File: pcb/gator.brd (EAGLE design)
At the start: 101.6 x 81.3 mm, 70 parts, among them J2 POWER_JACKPTH

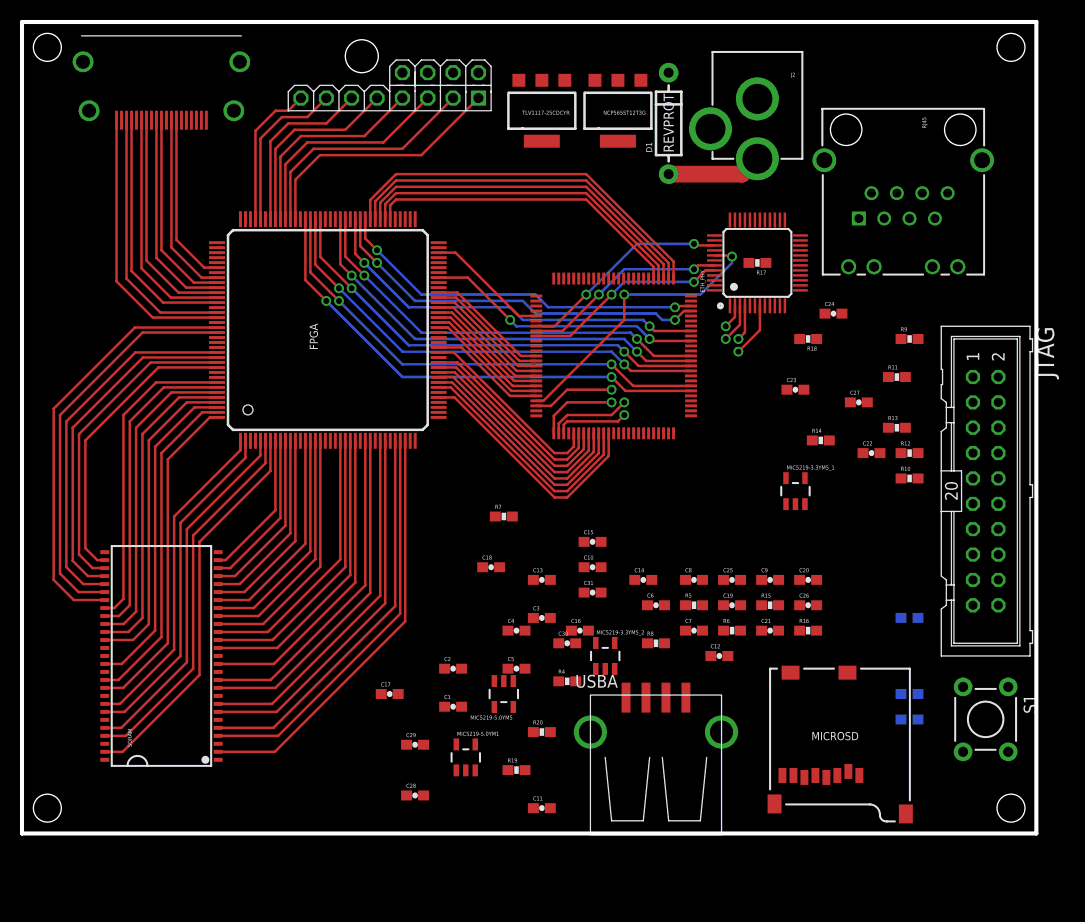
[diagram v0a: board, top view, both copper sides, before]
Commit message: Cleaned up power supplies and connected usb and micro sd
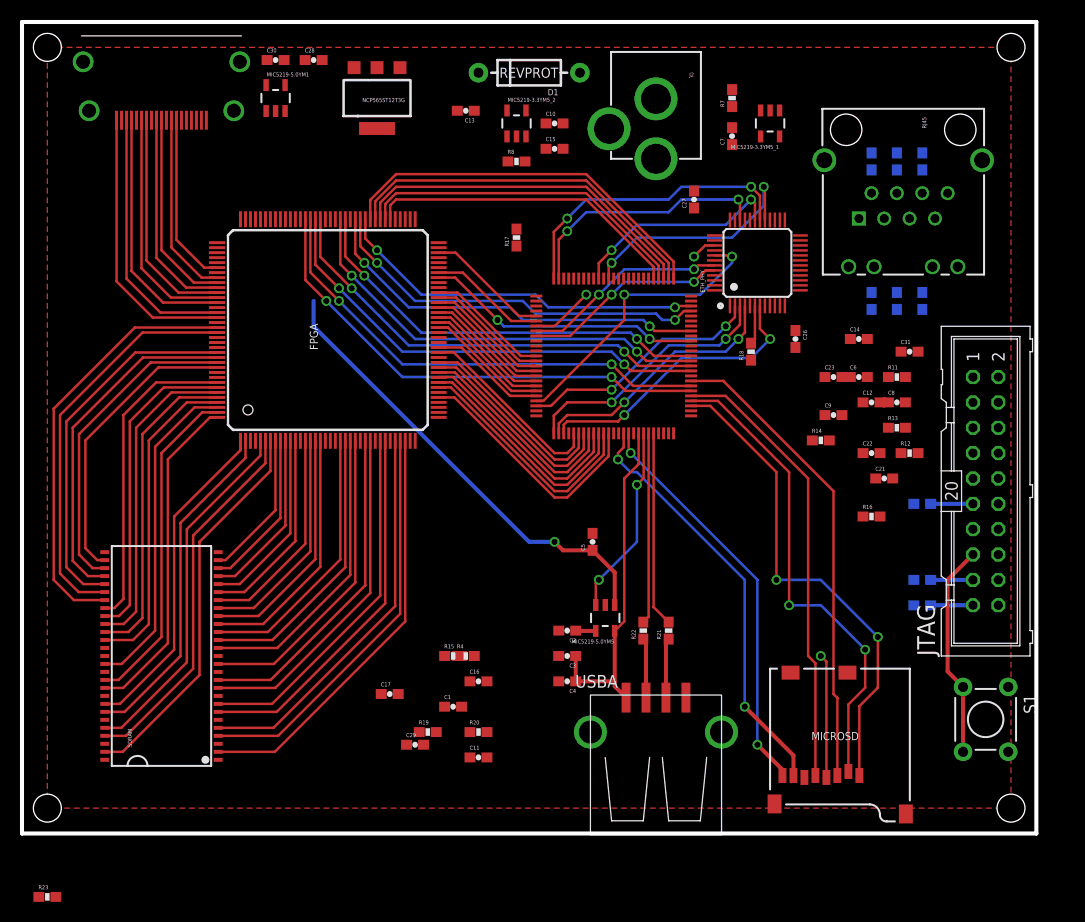
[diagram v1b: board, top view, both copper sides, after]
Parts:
- removed C18, C20: 100n, SparkFun-Passives:0603-CAP
- removed C19: 2.2u, SparkFun-Passives:0603-CAP
- removed TLV1117-25CDCYR: (no value), microbuilder:SOT223-R
- removed U$3: WING8, Papilio:WINGSIDE_8BIT
- added R21, R22: 22, SparkFun-Passives:0603-RES
- added R23: 10K, SparkFun-Passives:0603-RES
- moved C28 74.4 mm to (29.2, 77.5)
- moved MIC5219-5.0YM1 68.7 mm to (25.4, 73.7)
- moved C30 65.3 mm to (25.4, 77.5)
- moved MIC5219-3.3YM5_2 54.1 mm to (49.5, 71.1)
- moved R8 50.2 mm to (49.5, 67.3)
- moved R5 50.0 mm to (90.2, 67.3), flipped to the bottom, turned to 270 degrees
- moved R6 49.8 mm to (87.6, 67.3), flipped to the bottom, turned to 270 degrees
- moved C7 49.7 mm to (71.1, 69.8), turned to 90 degrees
- moved R7 47.7 mm to (71.1, 73.7), turned to 90 degrees
- moved C13 47.6 mm to (44.5, 72.4), turned to 180 degrees
- moved C10 44.6 mm to (53.3, 71.1)
- moved C25 44.2 mm to (85.1, 67.3), flipped to the bottom, turned to 90 degrees
- moved C31 39.9 mm to (88.9, 48.3)
- moved C15 39.6 mm to (53.3, 68.6)
- moved MIC5219-3.3YM5_1 36.9 mm to (74.9, 71.1), turned to 180 degrees
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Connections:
- removed net N$23: FPGA.P102, U$3.5
- removed net N$24: FPGA.P99, U$3.2
- removed net N$25: FPGA.P100, U$3.3
- removed net N$26: FPGA.P97, U$3.0
- removed net N$27: FPGA.P98, U$3.1
- removed net TCLK/SWCLK: JTAG.9
- removed net VCC/2: C19.1, C20.1, TLV1117-25CDCYR.2
- removed net VSS: U$1.10, U$1.27, U$1.74, U$1.99
- removed net VSSA: U$1.20
- new net SPI_MISO: FPGA.P66, U$1.31
- net +3V3: now also SDRAM.1, SDRAM.14, SDRAM.27, SDRAM.3, SDRAM.43, SDRAM.49, SDRAM.9
- net GND: now also SDRAM.12, SDRAM.28, SDRAM.41, SDRAM.46, SDRAM.52, SDRAM.54, SDRAM.6, U$1.10, U$1.20, U$1.27, U$1.74, U$1.99; no longer C18.2, C19.2, C20.2, TLV1117-25CDCYR.1
- net N$1: now also R21.2; no longer USBA.D+
- net N$19: now also R21.1, USBA.D+; no longer FPGA.P104, U$3.6
- net N$2: now also R22.2; no longer USBA.D-
- net N$20: now also R22.1, USBA.D-; no longer FPGA.P105, U$3.7
- net N$21: now also MIC5219-5.0YM1.3, R23.1; no longer FPGA.P101, U$3.4
- net TCK/SWCLK: now also JTAG.9
- net USB_EN: no longer MIC5219-5.0YM1.3
- net V+: now also R23.2; no longer C18.1, TLV1117-25CDCYR.3
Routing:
- net SD_D2: track 0.00 -> 49.3 mm, vias 0 -> 2
- net SD_D3: track 0.00 -> 48.5 mm, vias 0 -> 2
- net SD_CMD: track 0.00 -> 47.5 mm
- net V+: track 0.00 -> 46.2 mm, vias 0 -> 1
- net NRST: track 0.00 -> 46.0 mm, vias 0 -> 2
- net SD_CLK: track 0.00 -> 45.2 mm
- net SD_D0: track 0.00 -> 42.2 mm, vias 0 -> 2
- net SD_D1: track 0.00 -> 40.7 mm, vias 0 -> 2
- net USB_VBUS: track 0.00 -> 34.4 mm
- net MII_MDIO: track 0.00 -> 30.0 mm, vias 0 -> 2
- net N$26: track 25.7 -> 0.00 mm
- net 50MHZ_OSC: track 0.00 -> 25.7 mm, vias 0 -> 2
- net N$27: track 24.1 -> 0.00 mm
- net N$24: track 22.5 -> 0.00 mm
- net MII_MDC: track 0.00 -> 21.7 mm, vias 0 -> 2
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- added copper zone on layer 1, net GND

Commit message: more power supply cleanup
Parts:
- moved R23 83.1 mm to (29.2, 72.4)
- moved C11 62.2 mm to (44.5, 69.8), turned to 180 degrees
- moved R19 59.9 mm to (19.1, 66.0), turned to 90 degrees
- moved R20 59.1 mm to (17.8, 62.2)
- moved C16 55.0 mm to (27.9, 67.3)
- moved C6 51.8 mm to (41.9, 76.2), turned to 90 degrees
- moved R4 50.2 mm to (92.7, 3.81), turned to 180 degrees
- moved C21 34.3 mm to (64.8, 62.2), turned to 90 degrees
- moved R12 34.1 mm to (73.7, 68.6), turned to 180 degrees
- moved R16 33.9 mm to (77.5, 64.8)
- moved C9 33.1 mm to (78.7, 74.9), turned to 90 degrees
- moved R14 22.6 mm to (97.8, 53.3), turned to 270 degrees
- moved C17 16.1 mm to (41.9, 29.2)
- moved R13 13.3 mm to (91.4, 53.3), turned to 270 degrees
- moved R11 9.16 mm to (82.5, 53.3), turned to 270 degrees
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
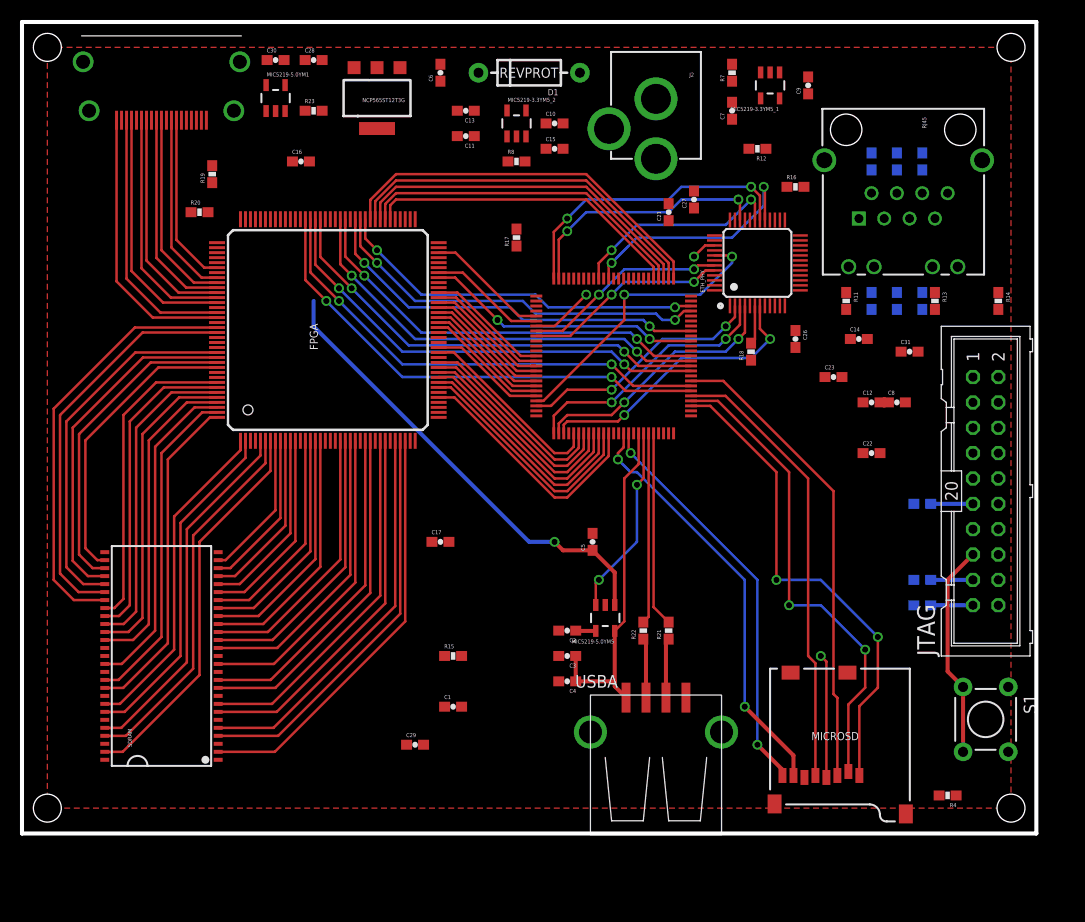
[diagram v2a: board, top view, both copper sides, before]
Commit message: Added HDMI termination, oscillators, improved routing
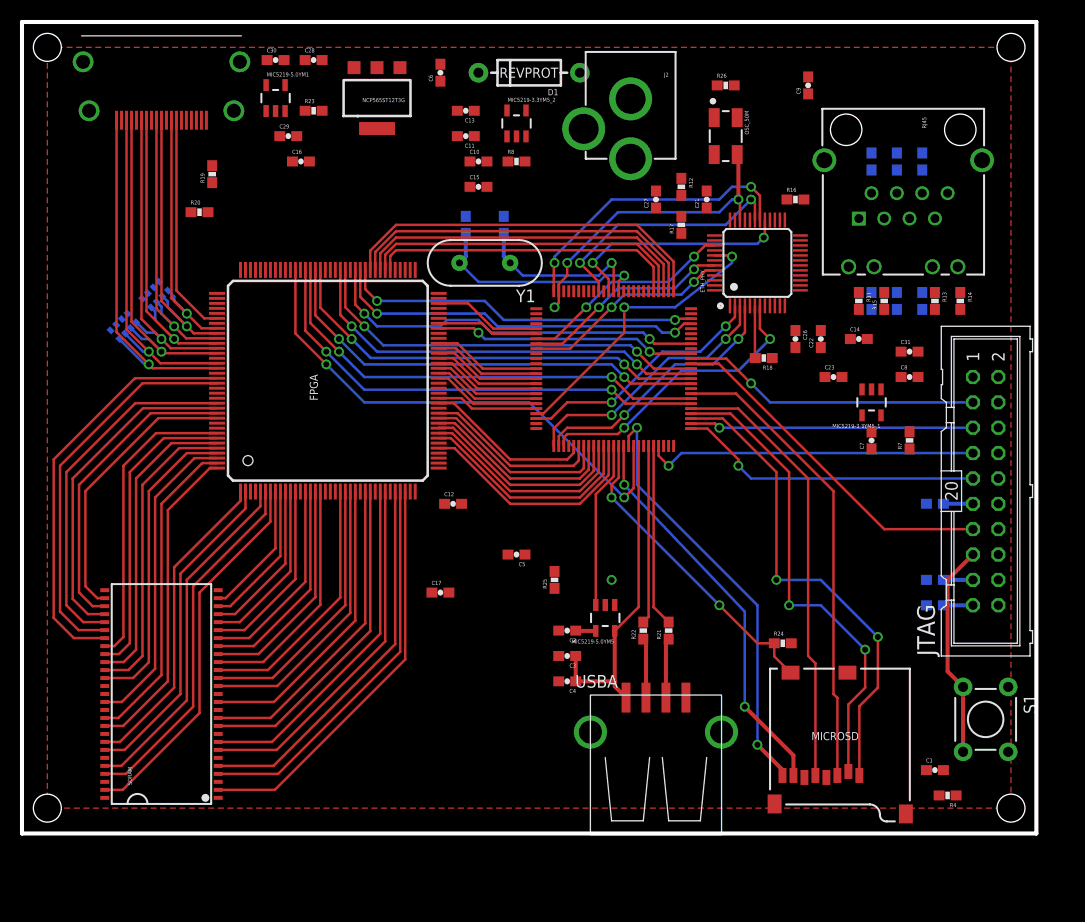
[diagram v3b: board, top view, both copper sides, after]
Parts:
- added C18, C19: 20p, SparkFun-Passives:0603-CAP
- added OSC_50M: OSCILLATOR5X3-PIN1-INDICATED, SparkFun-FreqCtrl:CRYSTAL-OSC-SMD-5X3
- added R24, R25: 10K, SparkFun-Passives:0603-RES
- added R26: 2K2, SparkFun-Passives:0603-RES
- added R27, R28: 51, SparkFun-Passives:0603-ARV
- added Y1: 12MHz, SparkFun-FreqCtrl:HC49US
- moved C29 62.3 mm to (26.7, 69.8)
- moved R15 55.9 mm to (86.4, 53.3), turned to 90 degrees
- moved C1 48.7 mm to (91.4, 6.35)
- moved C12 43.1 mm to (43.2, 33.0)
- moved R7 40.9 mm to (88.9, 39.4)
- moved C7 35.9 mm to (85.1, 39.4)
- moved MIC5219-3.3YM5_1 33.3 mm to (85.1, 43.2)
- moved R17 16.6 mm to (66.0, 61.0)
- moved C22 12.5 mm to (80.0, 49.5), turned to 90 degrees
- moved C10 8.52 mm to (45.7, 67.3)
- moved C15 8.52 mm to (45.7, 64.8)
- moved R12 8.52 mm to (66.0, 64.8), turned to 270 degrees
- moved C5 7.73 mm to (49.5, 27.9), turned to 180 degrees
- moved C17 5.08 mm to (41.9, 24.1)
- moved FPGA 5.08 mm to (30.6, 45.3)
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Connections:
- new net FPGA_CLK1: FPGA.P97, U$1.67
- new net FPGA_CLK2: FPGA.P98
- new net N$29: C18.1, U$1.12, Y1.2
- new net N$30: C19.1, U$1.13, Y1.1
- new net N$31: OSC_50M.1, R26.1
- new net SD_DETECT: MICROSD.CD1, R24.1, U$1.64
- net +3V3: now also OSC_50M.4, R24.2, R26.2; no longer FPGA.P103, FPGA.P122, FPGA.P125, FPGA.P129, FPGA.P135, FPGA.P18, FPGA.P20, FPGA.P31, FPGA.P36, FPGA.P4, FPGA.P42, FPGA.P53, FPGA.P63, FPGA.P76, FPGA.P86, FPGA.P90
- net 50MHZ_OSC: now also OSC_50M.3
- net GND: now also C18.2, C19.2, OSC_50M.2
- net TMDS_CLKN: now also R27.1
- net TMDS_CLKP: now also R27.2
- net TMDS_D0N: now also R27.3
- net TMDS_D0P: now also R27.4
- net TMDS_D1N: now also R28.1
- net TMDS_D1P: now also R28.2
- net TMDS_D2N: now also R28.3
- net TMDS_D2P: now also R28.4
- net USB_EN: now also R25.1, U$1.63; no longer U$1.69
- net V+: now also R25.2
- net VCCIO: now also FPGA.P103, FPGA.P122, FPGA.P125, FPGA.P129, FPGA.P135, FPGA.P18, FPGA.P20, FPGA.P31, FPGA.P36, FPGA.P4, FPGA.P42, FPGA.P53, FPGA.P63, FPGA.P76, FPGA.P86, FPGA.P90, R27.5, R27.6, R27.7, R27.8, R28.5, R28.6, R28.7, R28.8
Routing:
- net FPGA_CLK1: track 0.00 -> 51.7 mm, vias 0 -> 2
- net V+: track 46.2 -> 0.00 mm
- net TDO/SWO: track 0.00 -> 35.1 mm
- net TMS/SWDIO: track 0.00 -> 33.4 mm, vias 0 -> 1
- net SD_DETECT: track 0.00 -> 31.4 mm, vias 0 -> 2
- net TCK/SWCLK: track 0.00 -> 30.7 mm, vias 0 -> 1
- net /TRST: track 0.00 -> 30.1 mm, vias 0 -> 1
- net TDI: track 0.00 -> 28.4 mm, vias 0 -> 1
- net N$29: track 0.00 -> 22.6 mm, vias 0 -> 1
- net N$30: track 0.00 -> 17.4 mm, vias 0 -> 1
- net RMII_CRSDV: track 8.82 -> 21.7 mm
- net +3V3: track 12.4 -> 0.00 mm, vias 1 -> 0
- net TMDS_D0P: track 22.5 -> 31.6 mm, vias 0 -> 1
- net TMDS_D1P: track 25.0 -> 34.1 mm, vias 0 -> 1
- net TMDS_CLKP: track 19.9 -> 29.0 mm, vias 0 -> 1
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
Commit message: Routed power for SDRAM
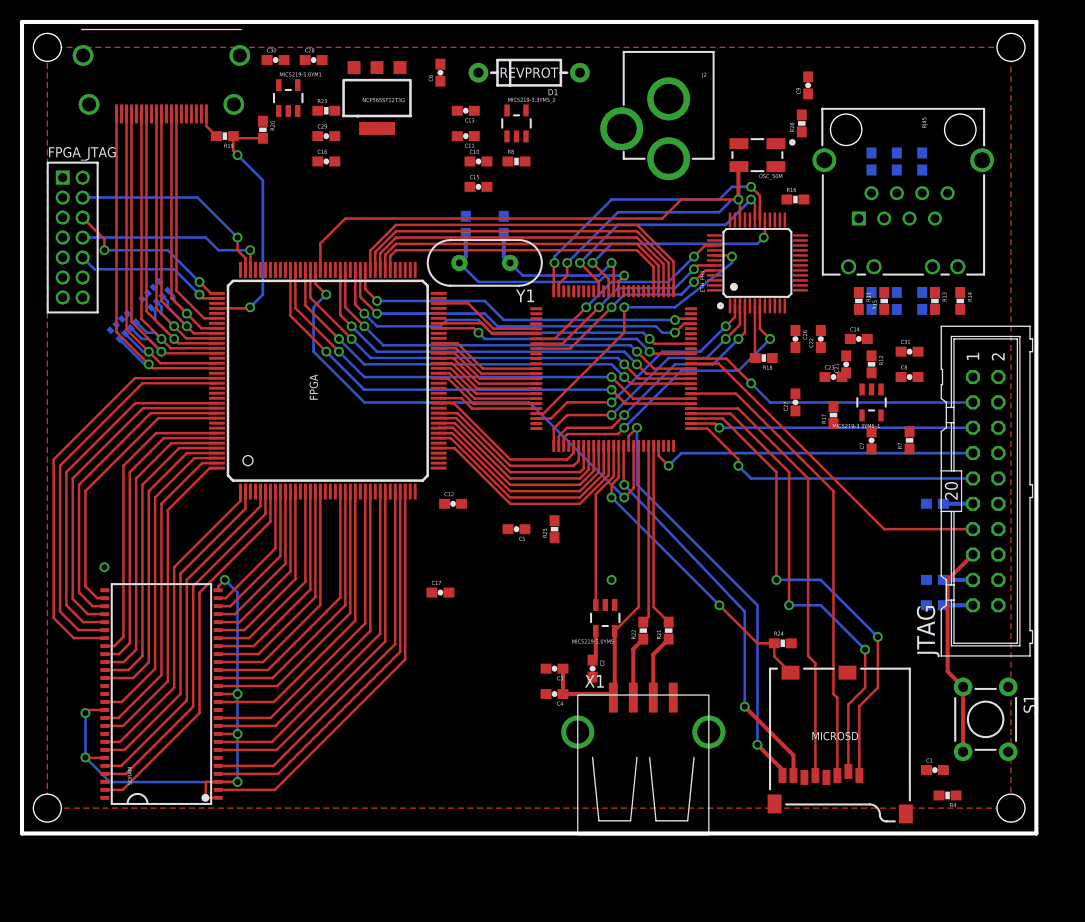
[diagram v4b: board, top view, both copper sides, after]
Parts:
- removed USBA: USB-A-S, SparkFun-Connectors:USB-A-S
- added FPGA_JTAG: 87758-14, con-molex-milli-grid:87758-14
- added X1: USB-A-S, SparkFun-Connectors:USB-A-S
- moved R12 26.1 mm to (85.1, 47.0)
- moved C27 24.7 mm to (77.5, 43.2)
- moved R17 24.4 mm to (81.3, 41.9)
- moved C21 21.6 mm to (82.5, 47.0)
- moved R20 10.4 mm to (24.1, 70.5), turned to 270 degrees
- moved R26 8.52 mm to (78.1, 71.1), turned to 90 degrees
- moved R25 5.08 mm to (53.3, 30.5)
- moved C2 4.58 mm to (57.1, 16.5), turned to 270 degrees
- moved R19 4.02 mm to (20.3, 69.8), turned to 180 degrees
- moved C29 3.81 mm to (30.5, 69.8)
- moved J2 3.81 mm to (64.8, 81.3)
- moved OSC_50M 3.70 mm to (73.7, 67.9), turned to 180 degrees
- moved C16 2.54 mm to (30.5, 67.3)
- moved C5 2.54 mm to (49.5, 30.5)
- moved C3 1.80 mm to (53.3, 16.5)
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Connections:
- removed net FPGA_CLK2: FPGA.P98
- new net FPGA_TCK: FPGA.P109, FPGA_JTAG.6
- new net FPGA_TDI: FPGA.P110, FPGA_JTAG.10
- new net FPGA_TDO: FPGA.P106, FPGA_JTAG.8
- new net FPGA_TMS: FPGA.P107, FPGA_JTAG.4
- net 50MHZ_OSC: now also FPGA.P92
- net D2: now also FPGA.P98; no longer FPGA.P95
- net D3: now also FPGA.P97; no longer FPGA.P94
- net DDC_CLK: now also U$2.P15; no longer FPGA.P115
- net DDC_DATA: now also U$2.P16; no longer FPGA.P111
- net FPGA_CLK1: now also FPGA.P93; no longer FPGA.P97
- net GND: now also FPGA.P73, FPGA_JTAG.11, FPGA_JTAG.13, FPGA_JTAG.3, FPGA_JTAG.5, FPGA_JTAG.7, FPGA_JTAG.9, X1.GND; no longer USBA.GND
- net N$19: now also X1.D+; no longer USBA.D+
- net N$20: now also X1.D-; no longer USBA.D-
- net NOE: now also FPGA.P95; no longer FPGA.P93
- net NWE: now also FPGA.P94; no longer FPGA.P92
- net USB_VBUS: now also X1.VBUS; no longer USBA.VBUS
- net VCCIO: now also FPGA_JTAG.2
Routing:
- net +3V3: track 0.00 -> 57.1 mm, vias 0 -> 6
- net 50MHZ_OSC: track 31.4 -> 74.7 mm, vias 3 -> 2
- net HDMI_DETECT: track 0.00 -> 25.3 mm, vias 0 -> 2
- net FPGA_TMS: track 0.00 -> 20.7 mm, vias 0 -> 1
- net FPGA_TDO: track 0.00 -> 19.3 mm, vias 0 -> 1
- net FPGA_TCK: track 0.00 -> 17.2 mm, vias 0 -> 2
- net FPGA_TDI: track 0.00 -> 15.1 mm, vias 0 -> 1
- net N$22: track 0.00 -> 2.64 mm
- net N$4: track 2.02 -> 3.06 mm
- net USB_VBUS: track 33.1 -> 34.0 mm
- net TMDS_D1P: track 34.1 -> 34.8 mm
- net TMDS_D2P: track 36.8 -> 37.4 mm
- net TMDS_D2N: track 34.6 -> 35.2 mm
- net TMDS_D1N: track 31.9 -> 32.5 mm
- net TMDS_D0P: track 31.6 -> 32.3 mm
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
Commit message: Routed some FPGA power and added back ground plane
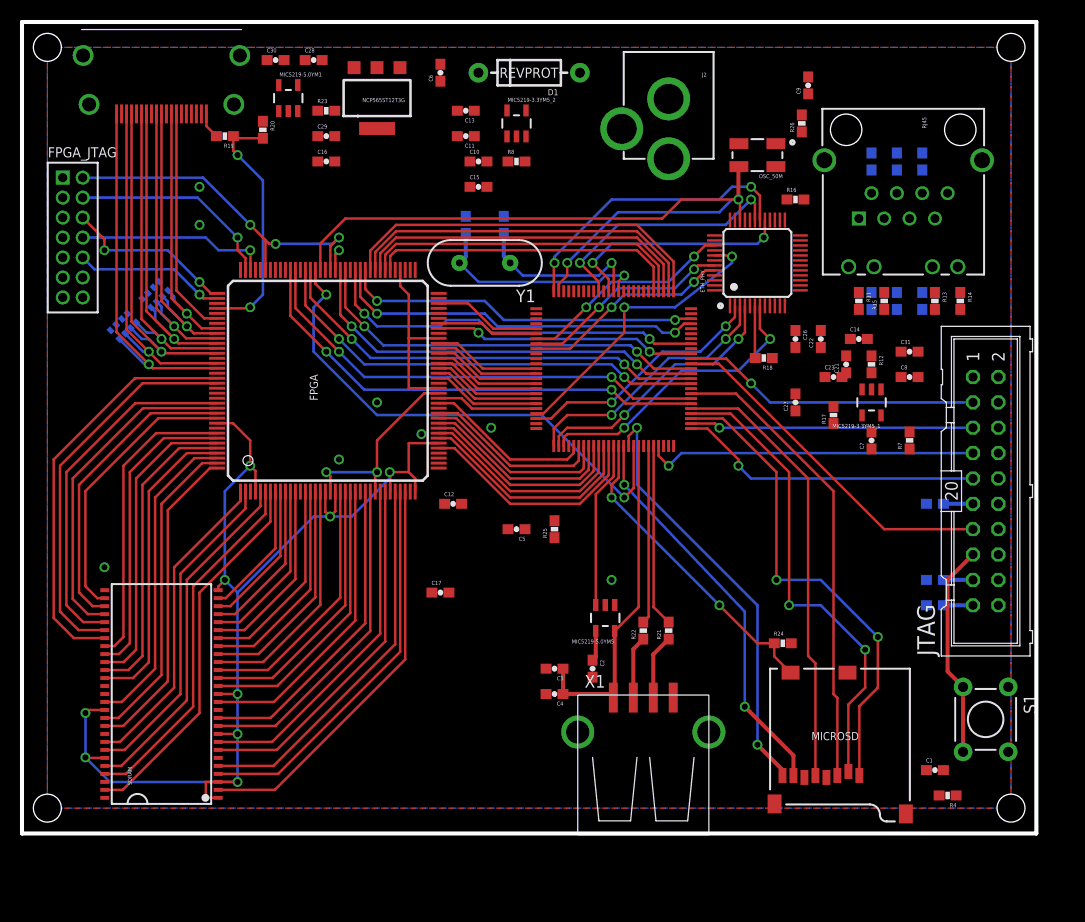
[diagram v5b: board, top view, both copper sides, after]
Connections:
- net +3V3: no longer SDRAM.1, SDRAM.14, SDRAM.27, SDRAM.3, SDRAM.43, SDRAM.49, SDRAM.9
- net VCCIO: now also SDRAM.1, SDRAM.14, SDRAM.27, SDRAM.3, SDRAM.43, SDRAM.49, SDRAM.9
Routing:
- net VCCIO: track 0.00 -> 170.4 mm, vias 0 -> 12
- net +3V3: track 57.1 -> 0.00 mm, vias 6 -> 0
- net VCCINT: track 0.00 -> 22.6 mm, vias 0 -> 3
- added copper zone on layer 16, net GND
